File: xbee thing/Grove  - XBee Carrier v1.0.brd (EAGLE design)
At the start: 46.5 x 50.9 mm, 44 parts, among them J1 SULLINS_NPPN101BFCN-RCSULLINS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, J2 HEADER-10P_STANDARD, J3 HEADER-10P_STANDARD, J4 SULLINS_NPPN101BFCN-RCSULLINS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, Q4 FQ7050B-6.000, U1 TUSB2046BVF, U2 RT9167A_33PB, U4 FT232RL

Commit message: add more resistors in series to Root D+ and D- pins
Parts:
- removed 5V, GND, PDM, PDP, USB2M, USB2P, XBM, XBP: (no value), wirepad:2,15/1,0
- added R16, R17: 27R, discrete:0603
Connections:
- new net N$5: R16.2, U1.2
- new net N1: R10.2, R17.2, U1.1
- net D+: no longer XBP.1
- net D-: no longer XBM.1
- net D_2+: no longer USB2P.1
- net D_2-: no longer USB2M.1
- net GND: now also U1.13, U1.17, U1.21, U1.9; no longer GND.1
- net ROOTD+: now also R17.1; no longer PDP.1, R10.2, U1.1
- net ROOTD-: now also R16.1; no longer PDM.1, U1.2
- net USB_5V: no longer 5V.1
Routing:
- net ROOTD+: track 67.5 -> 25.0 mm, vias 2 -> 0
- net D-: track 48.3 -> 11.5 mm
- net ROOTD-: track 60.8 -> 26.1 mm, vias 4 -> 2
- net D+: track 43.0 -> 9.56 mm
- net N1: track 0.00 -> 28.5 mm, vias 0 -> 2
- net N$5: track 0.00 -> 25.4 mm, vias 0 -> 2
- net D_2-: track 33.8 -> 28.2 mm
- net D_2+: track 28.4 -> 23.2 mm
- net USB_5V: track 84.5 -> 79.8 mm
- net GND: vias 4 -> 5

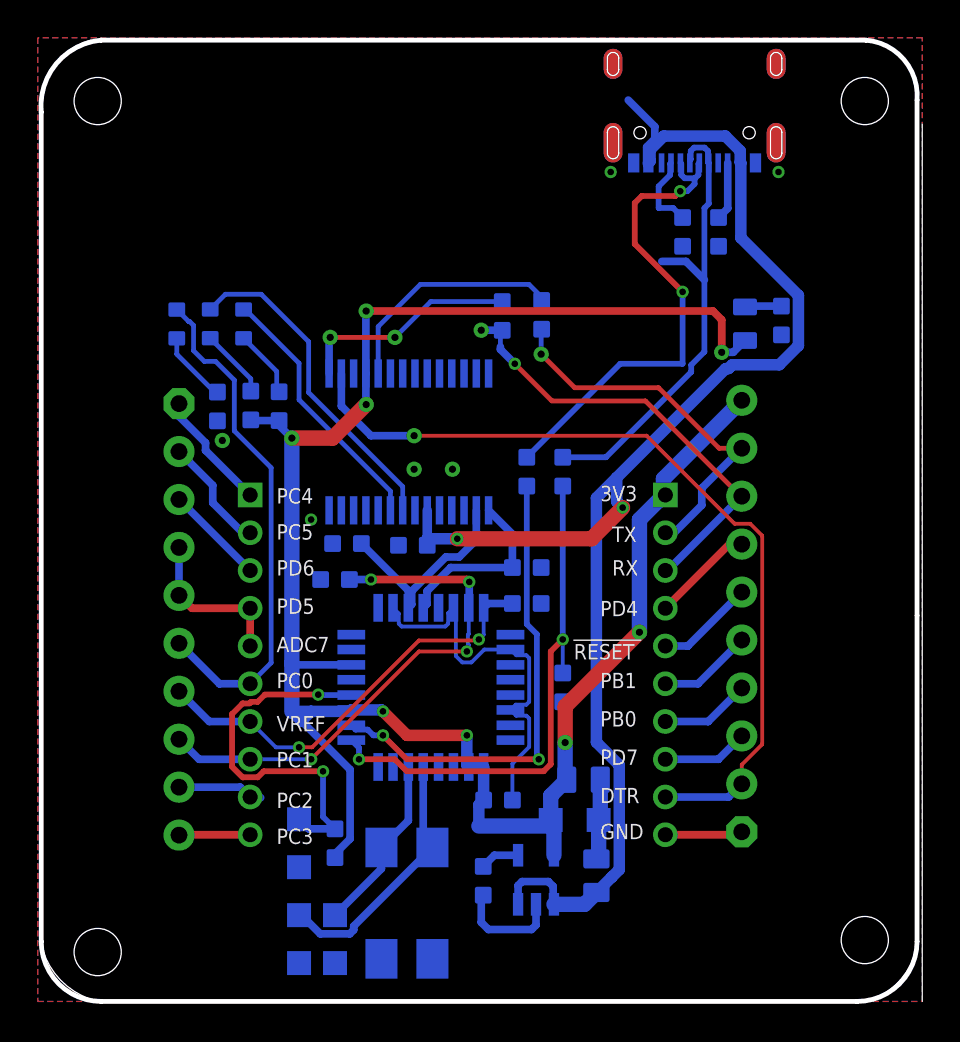
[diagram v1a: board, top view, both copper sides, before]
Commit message: make the ground plane actually a plane and not airwires
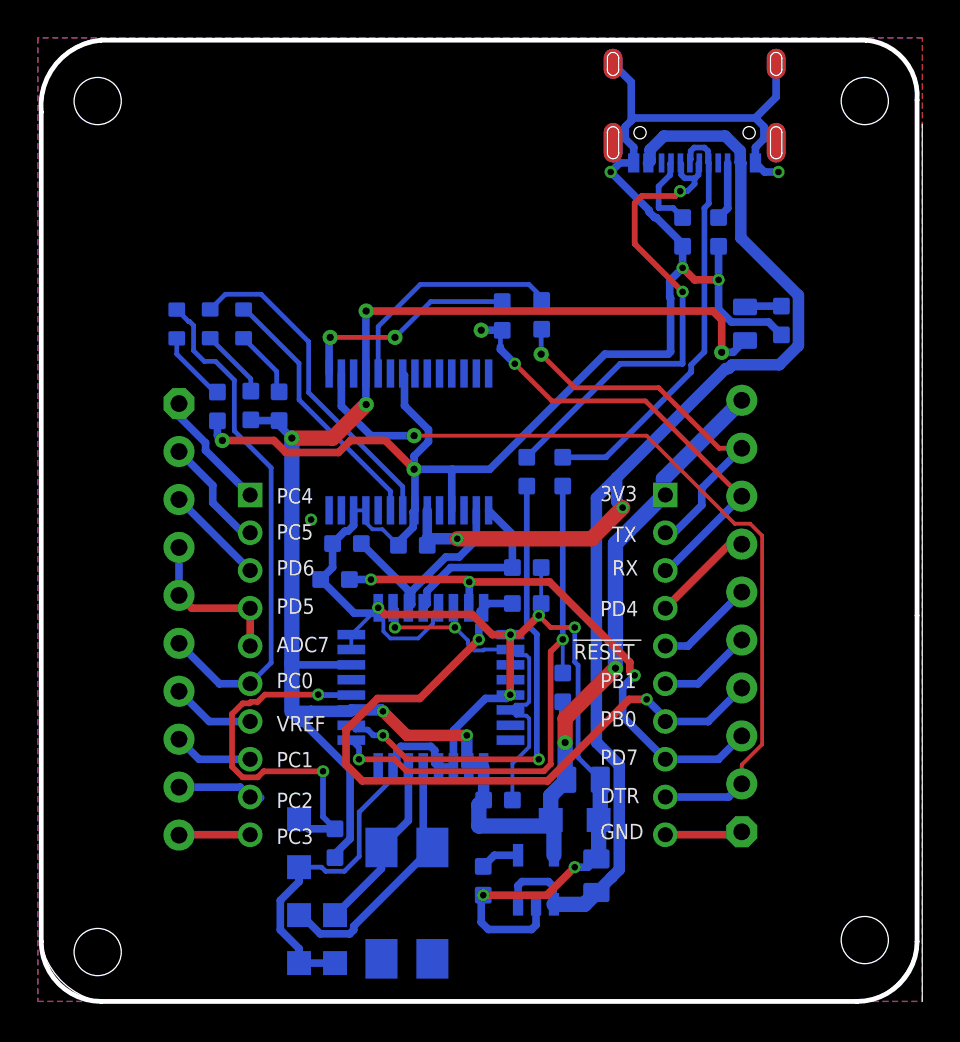
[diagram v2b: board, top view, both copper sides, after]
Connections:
- net D7: now also R8.2, U1.15
- net D8: now also R13.2, U1.16
- net D_2+: no longer R13.2, U1.16
- net D_2-: no longer R8.2, U1.15
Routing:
- net GND: track 10.0 -> 174.2 mm, vias 5 -> 13
- net D8: track 4.79 -> 38.7 mm, vias 0 -> 2
- net D7: track 4.57 -> 29.1 mm, vias 0 -> 3
- net D_2-: track 28.2 -> 4.21 mm, vias 4 -> 0
- net D_2+: track 23.2 -> 4.73 mm, vias 2 -> 0
- net USB_5V: track 79.8 -> 75.6 mm
- net ROOTD+: track 25.0 -> 22.4 mm
- net USB_OVRCUR: track 21.1 -> 19.5 mm, vias 0 -> 2
